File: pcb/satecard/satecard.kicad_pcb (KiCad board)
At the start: 2 copper layers, 64 x 30 mm, 2 parts, among them J1 SatellaviewEXT, J2 CF-CARD

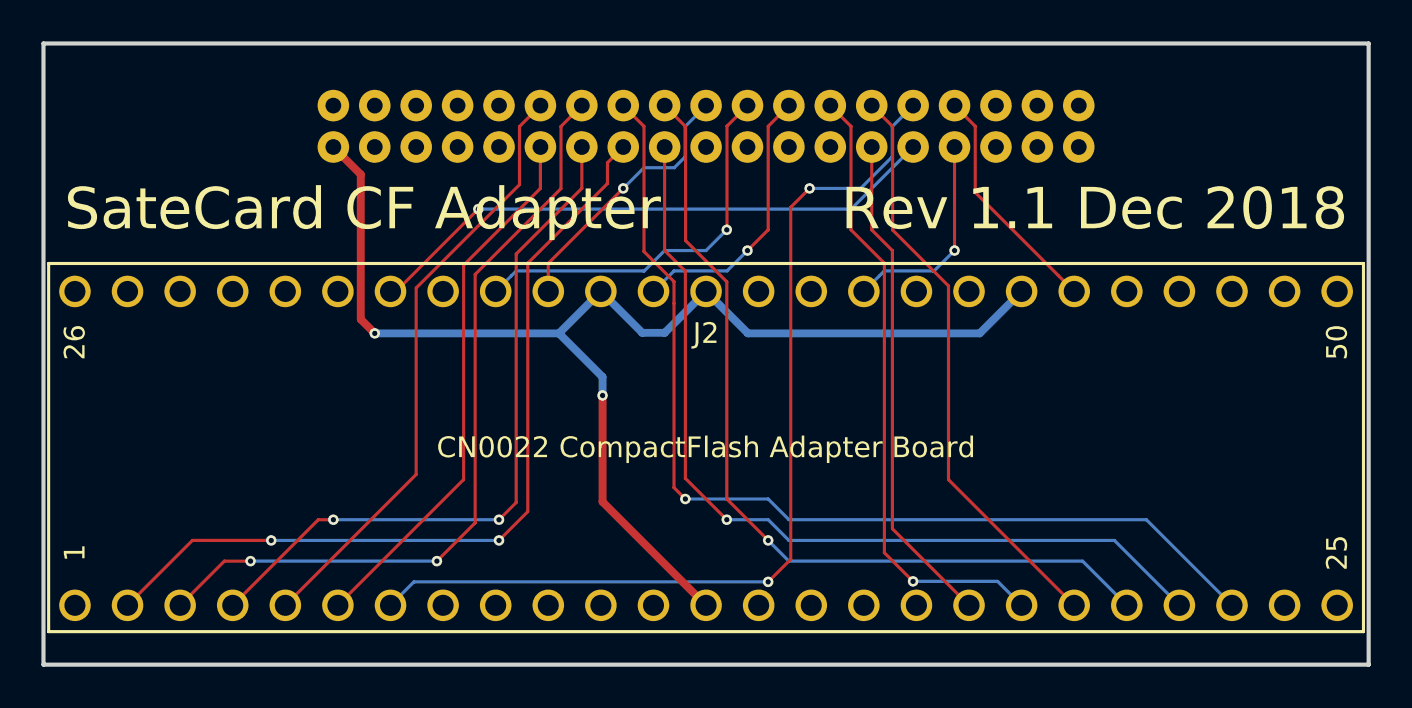
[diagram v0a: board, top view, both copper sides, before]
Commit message: rev 1.2: don't bother grounding the I/O pins
should reduce power consumption a bit and they're kind of pointless as a
detection mechanism anyway since you still have to attempt to
reset/configure the actual card
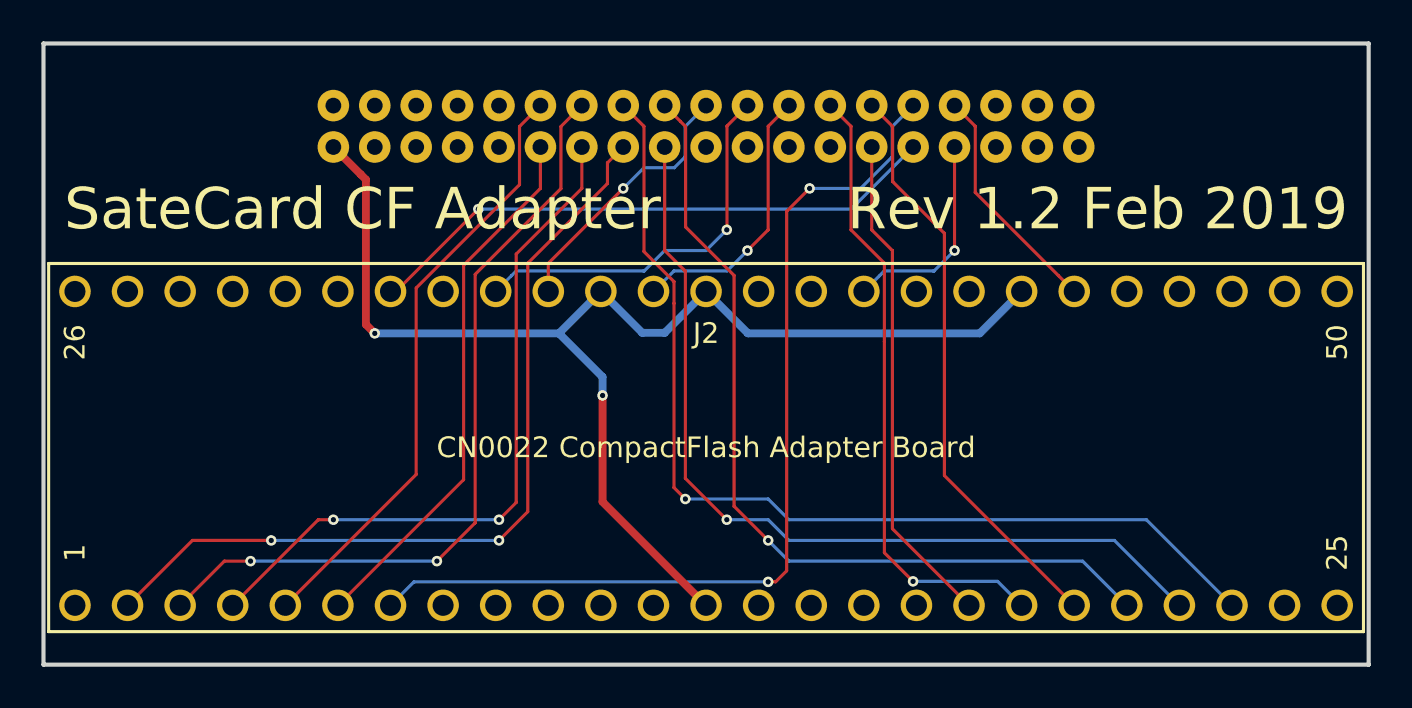
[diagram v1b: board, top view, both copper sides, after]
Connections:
- J1 pad 33: GND -> Net-(J1-Pad33)
- J1 pad 34: GND -> Net-(J1-Pad34)
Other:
- board text added: "Rev 1.2 Feb 2019"
- board text removed: "Rev 1.1 Dec 2018"
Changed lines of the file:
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@@
     (thickness 1.6)
     (drawings 7)
-    (tracks 158)
+    (tracks 160)
     (zones 0)
     (modules 2)
-    (nets 37)
+    (nets 39)
   )
   (page A4)
@@
   (net 35 /IRQ)
   (net 36 /LED)
+  (net 37 "Net-(J1-Pad33)")
+  (net 38 "Net-(J1-Pad34)")
   (net_class Default "This is the default net class."
     (clearance 0.1524)
@@
     (add_net /LED)
     (add_net GND)
+    (add_net "Net-(J1-Pad33)")
+    (add_net "Net-(J1-Pad34)")
     (add_net "Net-(J2-Pad24)")
     (add_net "Net-(J2-Pad25)")
@@
       (net 8 /!RESET))
     (pad 33 thru_hole circle (at -1 -13.93475 270) (size 1.524 1.524) (drill 0.762) (layers *.Cu *.Mask)
-      (net 9 GND))
+      (net 37 "Net-(J1-Pad33)"))
     (pad 34 thru_hole circle (at 1 -13.93475 270) (size 1.524 1.524) (drill 0.762) (layers *.Cu *.Mask)
-      (net 9 GND))
+      (net 38 "Net-(J1-Pad34)"))
     (pad 35 thru_hole circle (at -1 -15.93475 270) (size 1.524 1.524) (drill 0.762) (layers *.Cu *.Mask))
     (pad 36 thru_hole circle (at 1 -15.93475 270) (size 1.524 1.524) (drill 0.762) (layers *.Cu *.Mask)
@@
     (effects (font (size 2 2) (thickness 0.2)) (justify left))
   )
-  (gr_text "Rev 1.1 Dec 2018" (at 179 89) (layer F.SilkS)
+  (gr_text "Rev 1.2 Feb 2019" (at 179 89) (layer F.SilkS)
     (effects (font (size 2 2) (thickness 0.2)) (justify right))
   )
@@
   (segment (start 156.990601 85.009399) (end 156.990601 86.475489) (width 0.1524) (layer B.Cu) (net 1))
   (via (at 151 107) (size 0.508) (drill 0.254) (layers F.Cu B.Cu) (net 1))
-  (segment (start 152.089399 105.910601) (end 151 107) (width 0.1524) (layer F.Cu) (net 1))
-  (segment (start 153 88) (end 152.089399 88.910601) (width 0.1524) (layer F.Cu) (net 1))
-  (segment (start 152.089399 88.910601) (end 152.089399 105.910601) (width 0.1524) (layer F.Cu) (net 1))
   (segment (start 133.894999 107) (end 132.76 108.134999) (width 0.1524) (layer B.Cu) (net 1))
   (segment (start 151 107) (end 133.894999 107) (width 0.1524) (layer B.Cu) (net 1))
+  (segment (start 151.892 89.108) (end 153 88) (width 0.1524) (layer F.Cu) (net 1))
+  (segment (start 151.892 106.46721) (end 151.892 89.108) (width 0.1524) (layer F.Cu) (net 1))
+  (segment (start 151 107) (end 151.35921 107) (width 0.1524) (layer F.Cu) (net 1))
+  (segment (start 151.35921 107) (end 151.892 106.46721) (width 0.1524) (layer F.Cu) (net 1))
   (segment (start 156 90) (end 157 91) (width 0.1524) (layer F.Cu) (net 2))
   (segment (start 156 86) (end 156 90) (width 0.1524) (layer F.Cu) (net 2))
@@
   (segment (start 156.610601 95.389399) (end 156.610601 105.591734) (width 0.1524) (layer F.Cu) (net 3))
   (segment (start 156 84) (end 157.009399 85.009399) (width 0.1524) (layer F.Cu) (net 4))
-  (segment (start 157.009399 85.009399) (end 157.009399 90.009399) (width 0.1524) (layer F.Cu) (net 4))
-  (segment (start 157.009399 90.009399) (end 159.709399 92.709399) (width 0.1524) (layer F.Cu) (net 4))
-  (segment (start 159.709399 102.064398) (end 165.78 108.134999) (width 0.1524) (layer F.Cu) (net 4))
-  (segment (start 159.709399 92.709399) (end 159.709399 102.064398) (width 0.1524) (layer F.Cu) (net 4))
+  (segment (start 165.78 108.134999) (end 159.512 101.866999) (width 0.1524) (layer F.Cu) (net 4))
+  (segment (start 159.512 101.866999) (end 159.512 90.17) (width 0.1524) (layer F.Cu) (net 4))
+  (segment (start 157.009399 87.667399) (end 159.512 90.17) (width 0.1524) (layer F.Cu) (net 4))
+  (segment (start 157.009399 85.009399) (end 157.009399 87.667399) (width 0.1524) (layer F.Cu) (net 4))
   (segment (start 158 86) (end 157.009399 86.990601) (width 0.1524) (layer B.Cu) (net 5))
   (via (at 137 89) (size 0.508) (drill 0.254) (layers F.Cu B.Cu) (net 5))
@@
   (segment (start 159 92) (end 158.984398 91.984398) (width 0.1524) (layer B.Cu) (net 8))
   (via (at 132 95) (size 0.508) (drill 0.254) (layers F.Cu B.Cu) (net 10))
-  (segment (start 131.324901 94.324901) (end 132 95) (width 0.381) (layer F.Cu) (net 10))
   (segment (start 130 86) (end 131.324901 87.324901) (width 0.381) (layer F.Cu) (net 10))
-  (segment (start 131.324901 87.324901) (end 131.324901 94.324901) (width 0.381) (layer F.Cu) (net 10))
   (segment (start 140.894999 95) (end 142.92 92.974999) (width 0.381) (layer B.Cu) (net 10))
   (segment (start 132 95) (end 140.894999 95) (width 0.381) (layer B.Cu) (net 10))
@@
   (segment (start 143 103.134999) (end 148 108.134999) (width 0.381) (layer F.Cu) (net 10))
   (segment (start 143 98) (end 143 103.134999) (width 0.381) (layer F.Cu) (net 10))
+  (segment (start 132 95) (end 131.572 94.572) (width 0.381) (layer F.Cu) (net 10))
+  (segment (start 131.572 87.572) (end 131.324901 87.324901) (width 0.381) (layer F.Cu) (net 10))
+  (segment (start 131.572 94.572) (end 131.572 87.572) (width 0.381) (layer F.Cu) (net 10))
   (segment (start 138.990601 87.818308) (end 134 92.808909) (width 0.1524) (layer F.Cu) (net 27))
   (segment (start 140 84) (end 138.990601 85.009399) (width 0.1524) (layer F.Cu) (net 27))
@@
   (segment (start 139.389399 103.610601) (end 139.389399 91.610601) (width 0.1524) (layer F.Cu) (net 32))
   (segment (start 138 105) (end 139.389399 103.610601) (width 0.1524) (layer F.Cu) (net 32))
-  (segment (start 149 94) (end 149 103) (width 0.1524) (layer F.Cu) (net 33))
-  (segment (start 149 92.508909) (end 149 94) (width 0.1524) (layer F.Cu) (net 33))
-  (segment (start 147.009399 90.518308) (end 149 92.508909) (width 0.1524) (layer F.Cu) (net 33))
-  (segment (start 147.009399 85.009399) (end 147.009399 90.518308) (width 0.1524) (layer F.Cu) (net 33))
-  (segment (start 146 84) (end 147.009399 85.009399) (width 0.1524) (layer F.Cu) (net 33))
-  (segment (start 149 103) (end 151 105) (width 0.1524) (layer F.Cu) (net 33))
   (segment (start 151 105) (end 152 106) (width 0.1524) (layer B.Cu) (net 33))
   (via (at 151 105) (size 0.508) (drill 0.254) (layers F.Cu B.Cu) (net 33))
   (segment (start 166.185001 106) (end 168.32 108.134999) (width 0.1524) (layer B.Cu) (net 33))
   (segment (start 152 106) (end 166.185001 106) (width 0.1524) (layer B.Cu) (net 33))
+  (segment (start 151 105) (end 149.352 103.352) (width 0.1524) (layer F.Cu) (net 33))
+  (segment (start 149.352 103.352) (end 149.352 92.202) (width 0.1524) (layer F.Cu) (net 33))
+  (segment (start 146.761999 84.761999) (end 146 84) (width 0.1524) (layer F.Cu) (net 33))
+  (segment (start 147.009399 85.009399) (end 146.761999 84.761999) (width 0.1524) (layer F.Cu) (net 33))
+  (segment (start 147.009399 89.859399) (end 147.009399 85.009399) (width 0.1524) (layer F.Cu) (net 33))
+  (segment (start 149.352 92.202) (end 147.009399 89.859399) (width 0.1524) (layer F.Cu) (net 33))
   (segment (start 147 102) (end 147 92) (width 0.1524) (layer F.Cu) (net 34))
   (segment (start 147 92) (end 146 91) (width 0.1524) (layer F.Cu) (net 34))
